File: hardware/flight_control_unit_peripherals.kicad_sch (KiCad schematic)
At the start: 14 parts, among them J3 Conn_02x06_Odd_Even, J4 Conn_01x06, J5 Conn_01x04, J6 Conn_01x04, J7 Conn_02x10_Odd_Even, J8 Conn_01x10, U10 24CW1280T-I/OT, U11 AT45DB641E-SHN2B-T, U9 PCA9685PW

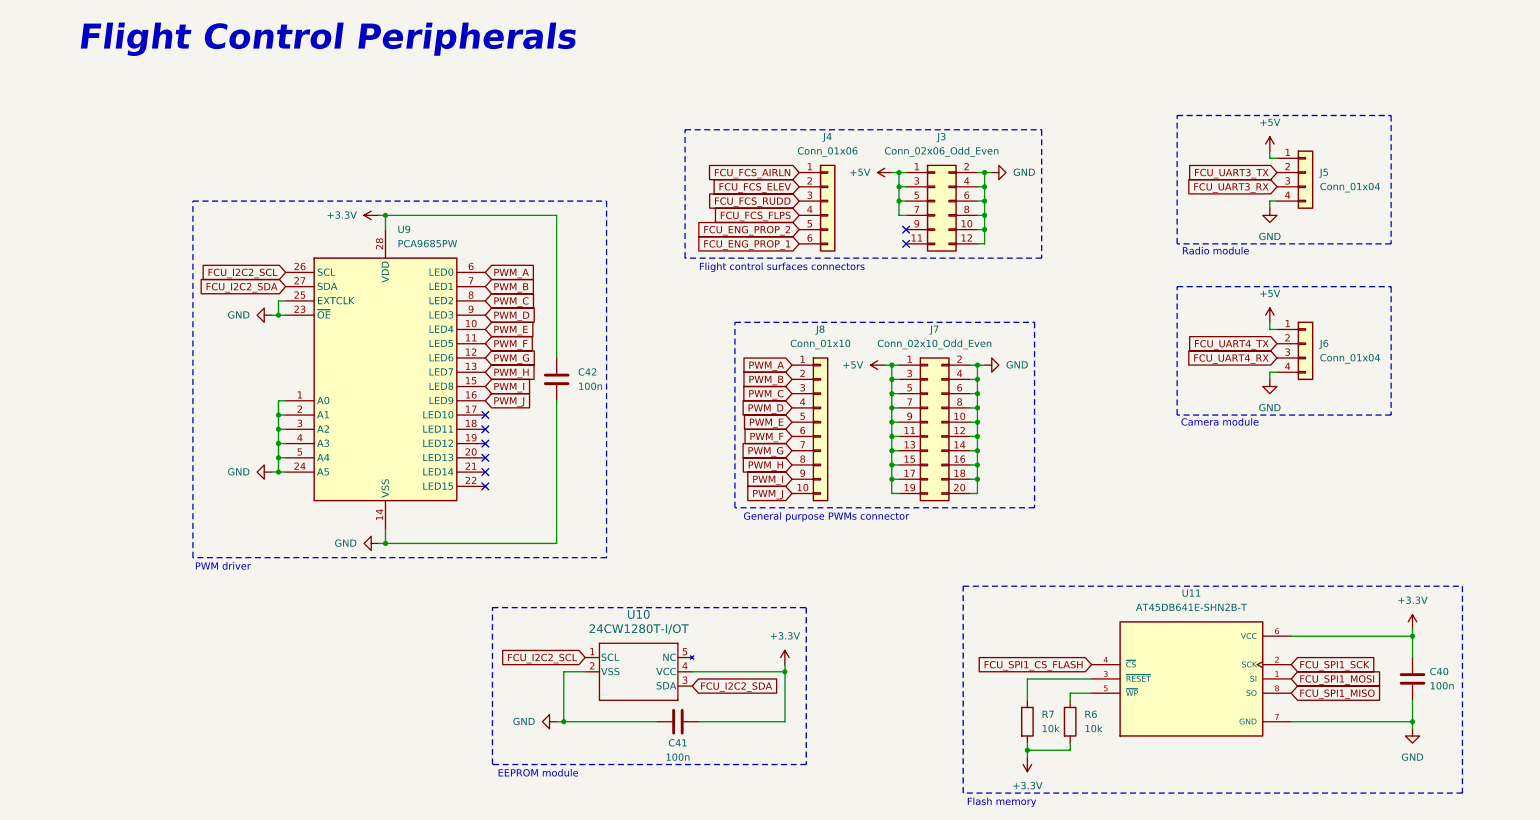
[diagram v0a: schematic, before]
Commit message: schematic and BOM done
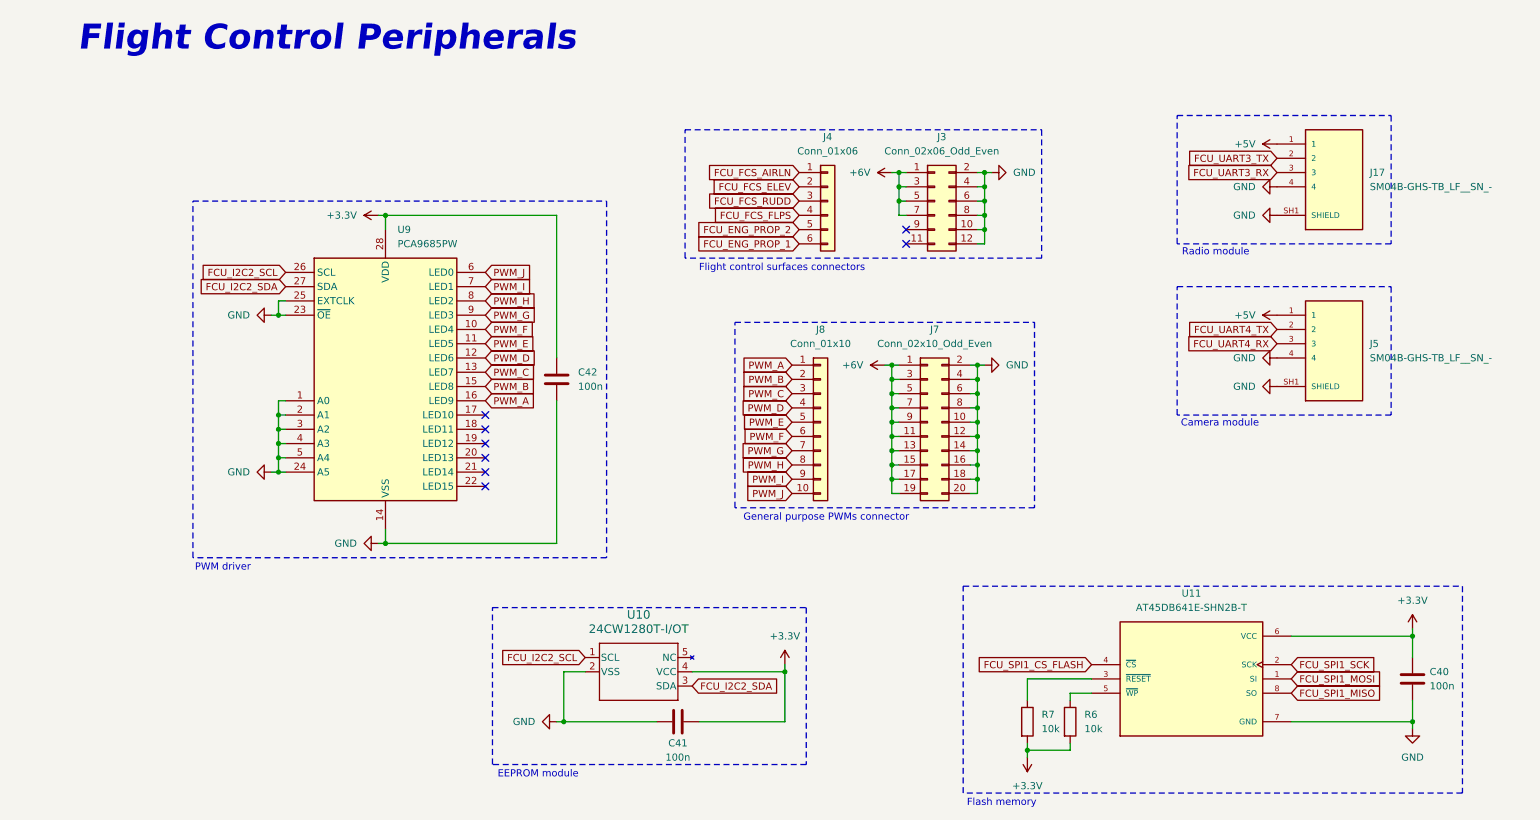
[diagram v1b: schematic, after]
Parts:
- removed J5, J6: Conn_01x04, symbol Connector_Generic:Conn_01x04
- added J17, J5: SM04B-GHS-TB_LF__SN_-, airplane:JST_SM04B-GHS-TB_LF__SN_-, symbol components:SM04B-GHS-TB_LF__SN_-
- C40, C41, C42: footprint (none) -> Capacitor_SMD:C_0603_1608Metric
- J3: footprint (none) -> Connector_PinHeader_2.54mm:PinHeader_2x06_P2.54mm_Vertical
- J4: footprint (none) -> Connector_PinHeader_2.54mm:PinHeader_1x06_P2.54mm_Vertical
- J7: footprint (none) -> Connector_PinHeader_2.54mm:PinHeader_2x10_P2.54mm_Vertical
- J8: footprint (none) -> Connector_PinHeader_2.54mm:PinHeader_1x10_P2.54mm_Vertical
- R6, R7: footprint (none) -> Resistor_SMD:R_0603_1608Metric
- U10: footprint SOT-23-5_2P9X1P6_MCH -> airplane:SOT-23-5_2P9X1P6_MCH; Manufacturer Part Number (none) -> 24CW1280T-I/OT
- U11: footprint AT45DB641E-SHN2B-T:SOIC127P798X216-8N -> airplane:SOIC127P798X216-8N; Manufacturer Part Number (none) -> AT45DB641E-SHN2B-T
- U9: Manufacturer Part Number (none) -> PCA9685PW,118
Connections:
- net +5V: now also J17.1, J5.1; no longer J3.1 (Pin_1), J3.3 (Pin_3), J3.5 (Pin_5), J3.7 (Pin_7), J7.1 (Pin_1), J7.11 (Pin_11), J7.13 (Pin_13), J7.15 (Pin_15), J7.17 (Pin_17), J7.19 (Pin_19), J7.3 (Pin_3), J7.5 (Pin_5), J7.7 (Pin_7), J7.9 (Pin_9)
- net FCU_UART3_RX: now also J17.3
- net FCU_UART3_TX: now also J17.2
- net FCU_UART4_RX: now also J5.3
- net FCU_UART4_TX: now also J5.2
- net GND: now also J17.4, J17.SH1 (SHIELD), J17.SH2 (SHIELD), J5.4, J5.SH1 (SHIELD), J5.SH2 (SHIELD)
- net PWM_A: now also U9.16 (LED9); no longer U9.6 (LED0)
- net PWM_B: now also U9.15 (LED8); no longer U9.7 (LED1)
- net PWM_C: now also U9.13 (LED7); no longer U9.8 (LED2)
- net PWM_D: now also U9.12 (LED6); no longer U9.9 (LED3)
- net PWM_E: now also U9.11 (LED5); no longer U9.10 (LED4)
- net PWM_F: now also U9.10 (LED4); no longer U9.11 (LED5)
- net PWM_G: now also U9.9 (LED3); no longer U9.12 (LED6)
- net PWM_H: now also U9.8 (LED2); no longer U9.13 (LED7)
- net PWM_I: now also U9.7 (LED1); no longer U9.15 (LED8)
- net PWM_J: now also U9.6 (LED0); no longer U9.16 (LED9)
- new net +6V: J3.1 (Pin_1), J3.3 (Pin_3), J3.5 (Pin_5), J3.7 (Pin_7), J7.1 (Pin_1), J7.11 (Pin_11), J7.13 (Pin_13), J7.15 (Pin_15), J7.17 (Pin_17), J7.19 (Pin_19), J7.3 (Pin_3), J7.5 (Pin_5), J7.7 (Pin_7), J7.9 (Pin_9)
